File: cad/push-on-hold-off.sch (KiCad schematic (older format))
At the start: 17 parts, among them P1 CONN_01X04, P2 CONN_01X04, Q1 IRF7309IPBF, SW1 SW_PUSH_SMALL

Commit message: Sort button-side of board
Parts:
- LED1, LED2: footprint KiCad/LEDs.pretty:LED_0603 -> KiCad/Resistors_SMD.pretty:R_0603_HandSoldering
- Q1: footprint Housings_SOIC:SOIC-8_3.9x4.9mm_Pitch1.27mm -> KiCad/Housings_SOIC.pretty:SOIC-8_3.9x4.9mm_Pitch1.27mm
- SW1: footprint KiCad/Buttons_Switches_SMD.pretty:SW_SPST_EVPBF -> custom:FSM2JSMA
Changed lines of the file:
@@
 F 0 "Q1" H 5900 4250 50  0000 L CNN
 F 1 "IRF7309IPBF" H 5600 4550 50  0000 L CNN
-F 2 "Housings_SOIC:SOIC-8_3.9x4.9mm_Pitch1.27mm" H 5200 3700 50  0000 L CNN
+F 2 "KiCad/Housings_SOIC.pretty:SOIC-8_3.9x4.9mm_Pitch1.27mm" H 5200 3700 50  0000 L CNN
 F 3 "" H 6050 4400 50  0000 L CNN
 F 4 "2468006" H 6050 4400 60  0001 C CNN "Vendor"
@@
 F 0 "Q1" H 6250 3775 50  0000 L CNN
 F 1 "IRF7309IPBF" H 6250 3700 50  0000 L CNN
-F 2 "Housings_SOIC:SOIC-8_3.9x4.9mm_Pitch1.27mm" H 6250 3625 50  0000 L CNN
+F 2 "KiCad/Housings_SOIC.pretty:SOIC-8_3.9x4.9mm_Pitch1.27mm" H 6250 3625 50  0000 L CNN
 F 3 "" H 6000 3700 50  0000 L CNN
 	2    6000 3700
@@
 $EndComp
 $Comp
-L GND #PWR1
+L GND #PWR01
 U 1 1 569FC7CE
 P 3550 4150
-F 0 "#PWR1" H 3550 3900 50  0001 C CNN
+F 0 "#PWR01" H 3550 3900 50  0001 C CNN
 F 1 "GND" H 3550 4000 50  0000 C CNN
 F 2 "" H 3550 4150 60  0000 C CNN
@@
 $EndComp
 $Comp
-L GND #PWR3
+L GND #PWR02
 U 1 1 569FCD58
 P 5950 4650
-F 0 "#PWR3" H 5950 4400 50  0001 C CNN
+F 0 "#PWR02" H 5950 4400 50  0001 C CNN
 F 1 "GND" H 5950 4500 50  0000 C CNN
 F 2 "" H 5950 4650 60  0000 C CNN
@@
 Button
 $Comp
-L GND #PWR6
+L GND #PWR03
 U 1 1 569FDE5F
 P 7650 4050
-F 0 "#PWR6" H 7650 3800 50  0001 C CNN
+F 0 "#PWR03" H 7650 3800 50  0001 C CNN
 F 1 "GND" H 7650 3900 50  0000 C CNN
 F 2 "" H 7650 4050 60  0000 C CNN
@@
 F 0 "SW1" H 6100 5460 30  0000 C CNN
 F 1 "SW_PUSH_SMALL" H 5950 5271 30  0000 C CNN
-F 2 "KiCad/Buttons_Switches_SMD.pretty:SW_SPST_EVPBF" H 5950 5350 60  0001 C CNN
+F 2 "custom:FSM2JSMA" H 5950 5350 60  0001 C CNN
 F 3 "" H 5950 5350 60  0000 C CNN
 F 4 "3801305" H 5950 5350 60  0001 C CNN "Vendor"
@@
 $EndComp
 $Comp
-L GND #PWR4
+L GND #PWR04
 U 1 1 569FECE2
 P 6100 5500
-F 0 "#PWR4" H 6100 5250 50  0001 C CNN
+F 0 "#PWR04" H 6100 5250 50  0001 C CNN
 F 1 "GND" H 6100 5350 50  0000 C CNN
 F 2 "" H 6100 5500 60  0000 C CNN
@@
 F 0 "LED2" V 7296 4492 50  0000 R CNN
 F 1 "LED" V 7205 4492 50  0000 R CNN
-F 2 "KiCad/LEDs.pretty:LED_0603" H 7250 4600 50  0001 C CNN
+F 2 "KiCad/Resistors_SMD.pretty:R_0603_HandSoldering" H 7250 4600 50  0001 C CNN
 F 3 "" H 7250 4600 50  0000 C CNN
 	1    7250 4600
@@
 F 0 "LED1" V 3796 4742 50  0000 R CNN
 F 1 "LED" V 3705 4742 50  0000 R CNN
-F 2 "KiCad/LEDs.pretty:LED_0603" H 3750 4850 50  0001 C CNN
+F 2 "KiCad/Resistors_SMD.pretty:R_0603_HandSoldering" H 3750 4850 50  0001 C CNN
 F 3 "" H 3750 4850 50  0000 C CNN
 	1    3750 4850
@@
 	3750 4500 3750 4650
 $Comp
-L GND #PWR5
+L GND #PWR05
 U 1 1 57595997
 P 7250 5000
-F 0 "#PWR5" H 7250 4750 50  0001 C CNN
+F 0 "#PWR05" H 7250 4750 50  0001 C CNN
 F 1 "GND" H 7255 4827 50  0000 C CNN
 F 2 "" H 7250 5000 50  0000 C CNN
@@
 $EndComp
 $Comp
-L GND #PWR2
+L GND #PWR06
 U 1 1 575959DF
 P 3750 5150
-F 0 "#PWR2" H 3750 4900 50  0001 C CNN
+F 0 "#PWR06" H 3750 4900 50  0001 C CNN
 F 1 "GND" H 3755 4977 50  0000 C CNN
 F 2 "" H 3750 5150 50  0000 C CNN

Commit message: Switch diode to a mini-melf
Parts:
- D1: footprint KiCad/Diodes_SMD.pretty:SMA_Handsoldering -> KiCad/Diodes_SMD.pretty:MiniMELF_Handsoldering
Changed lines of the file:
@@
 F 0 "D1" H 4000 4600 50  0000 C CNN
 F 1 "D" H 4000 4400 50  0000 C CNN
-F 2 "KiCad/Diodes_SMD.pretty:SMA_Handsoldering" H 4000 4500 60  0001 C CNN
+F 2 "KiCad/Diodes_SMD.pretty:MiniMELF_Handsoldering" H 4000 4500 60  0001 C CNN
 F 3 "" H 4000 4500 60  0000 C CNN
 F 4 "1466524" H 4000 4500 60  0001 C CNN "Vendor"

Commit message: Route the board
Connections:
- net Vin: no longer C4.1, JP1.2
- new net: C4.1, JP1.2
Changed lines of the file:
@@
 	5400 3900 5500 3900
 Connection ~ 5950 3900
-Wire Wire Line
-	5450 3600 5450 3900
 Connection ~ 5450 3900
 Connection ~ 5450 3600

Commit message: Sort out silkscreen and plot
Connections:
- net Vin: now also C4.1, JP1.2
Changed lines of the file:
@@
 	3750 5150 3750 5050
 Connection ~ 3750 3600
+Wire Wire Line
+	5450 3900 5450 3600
 $EndSCHEMATC

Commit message: Update BOM
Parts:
- C1: Description (none) -> 1uF 0603 X5R; Digikey (none) -> 445-1796-1-ND; Farnell (none) -> 2354048; Manufacturer (none) -> TDK; Mouser (none) -> CC0603KRX5R7BB105; Newark (none) -> 04X3188; Part Number (none) -> C0603X5R0J104K030BC; RS (none) -> 7882818
- C2: Description (none) -> 10uF 0603 X5R; Digikey (none) -> 445-6853-1-ND; Farnell (none) -> 2211164; Manufacturer (none) -> TDK; Mouser (none) -> 06036D106MAT2A; Newark (none) -> 04X3239; Part Number (none) -> C1608X5R1A106M080AC; RS (none) -> 7882893
- D1: Farnell (none) -> 7355513; Manufacturer (none) -> MULTICOMP; Part Number (none) -> LL4148
- Q1: Digikey (none) -> IRF7309PBFCT-ND; Farnell (none) -> 2468006; Manufacturer (none) -> International Rectifier; Mouser (none) -> IRF7309PBF; Newark (none) -> 19K8239; Part Number (none) -> IRF7309PBF; RS (none) -> 5429377
- R1: Description (none) -> 10k 0603; Digikey (none) -> 541-10KGCT-ND; Farnell (none) -> 1469749; Manufacturer (none) -> Vishay; Mouser (none) -> CRCW060310K0JNEAHP; Newark (none) -> 52K8066; Part Number (none) -> CRCW060310K0JNEA; RS (none) -> 8206928
- R2: Description (none) -> 100k 0603; Digikey (none) -> 541-100KGCT-ND; Farnell (none) -> 1692517; Manufacturer (none) -> Vishay; Mouser (none) -> CRCW0603100KJNEAHP; Newark (none) -> 59M6763; Part Number (none) -> CRCW0603100KJNEA; RS (none) -> 8206916
- R3: Description (none) -> 300k 0603; Digikey (none) -> 311-300KGRCT-ND; Farnell (none) -> 1652871; Manufacturer (none) -> Vishay; Mouser (none) -> RC0603JR07300KL; Newark (none) -> 52K8409; Part Number (none) -> CRCW0603300KFKEA; RS (none) -> 8280617
- SW1: Digikey (none) -> 450-1129-ND; Farnell (none) -> 3801305; Manufacturer (none) -> TE Connectivity; Mouser (none) -> 414375651; Newark (none) -> 93K3887; Part Number (none) -> 4-1437565-1; RS (none) -> 4791508

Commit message: Extract bom into schematic
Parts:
- C1: Digikey 445-1796-1-ND -> 490-3290-1-ND; Farnell 2354048 -> 1828900; MPN (none) -> GRM188R71E224KA88D; Manufacturer TDK -> Murata; Mouser CC0603KRX5R7BB105 -> GRM188R71E224KA88D; Newark 04X3188 -> 91R0949; Qty (none) -> 1; RS 7882818 -> 6242496
- C2: MPN (none) -> C1608X5R1A106M080AC; Qty (none) -> 1
- C4: Description (none) -> 0.1uF 0603 X5R; Digikey (none) -> 399-5089-1-ND; Farnell (none) -> 1288255; MPN (none) -> C0603C104K5RACTU; Manufacturer (none) -> Kemet; Mouser (none) -> C0603C104K5RACTU; Newark (none) -> 72J5992; Qty (none) -> 1; RS (none) -> 8015347
- D1: Description (none) -> Diode MiniMELF; Digikey (none) -> LL4148FSCT-ND; MPN (none) -> LL4148; Manufacturer MULTICOMP -> (none); Mouser (none) -> LL4148; Newark (none) -> 14M6003; Qty (none) -> 1; RS (none) -> 6708826
- LED1, LED2: Description (none) -> 0603 20mA yellow; Digikey (none) -> 511-1582-1-ND; Farnell (none) -> 1465989; MPN (none) -> SML-D12Y8WT86; Manufacturer (none) -> Rohm; Mouser (none) -> 5988150107F; Newark (none) -> 75R0585; Qty (none) -> 2; RS (none) -> 7008023
- Q1: Description (none) -> 30V Vds, 3A Id, Dual HEXFET MOSFET; MPN (none) -> IRF7309PBF; Qty (none) -> 1
- R1: MPN (none) -> CRCW060310K0JNEA; Qty (none) -> 1
- R2: MPN (none) -> CRCW0603100KJNEA; Qty (none) -> 2
- R3: MPN (none) -> CRCW0603300KFKEA; Qty (none) -> 1
- R4: Description (none) -> 100k 0603; Digikey (none) -> 541-100KGCT-ND; Farnell (none) -> 1692517; MPN (none) -> CRCW0603100KJNEA; Manufacturer (none) -> Vishay; Mouser (none) -> CRCW0603100KJNEAHP; Newark (none) -> 59M6763; Qty (none) -> 2; RS (none) -> 8206916
- R5: Description (none) -> 1k 0603; Digikey (none) -> 311-1.00KCRCT-ND; Farnell (none) -> 9237496; MPN (none) -> RC0805FR-071KL; Manufacturer (none) -> Yageo; Mouser (none) -> RC0805FR071KL; Newark (none) -> 82K7536; Qty (none) -> 2; RS (none) -> 6183583
- SW1: Description (none) -> Tactile switch; Digikey 450-1129-ND -> 450-1130-ND; Farnell 3801305 -> 3801287; MPN (none) -> FSM2JSMA; Manufacturer TE Connectivity -> (none); Mouser 414375651 -> 214375657; Newark 93K3887 -> 92F2864; Qty (none) -> 1; RS 4791508 -> 4791491

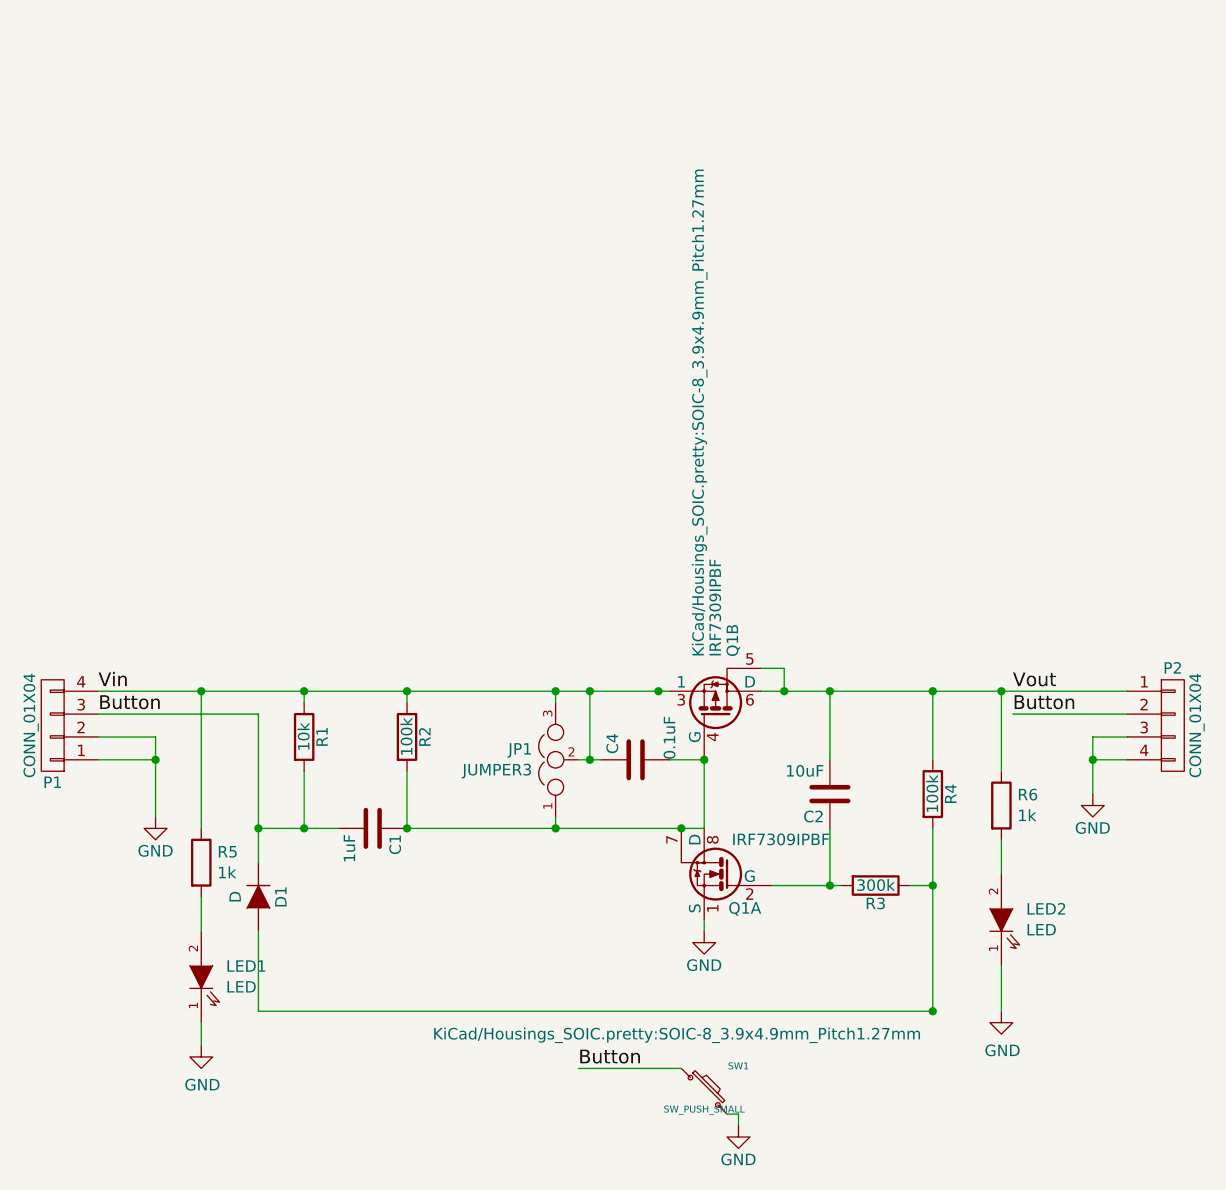
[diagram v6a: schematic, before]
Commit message: Fix auto-on jumper which was supposed to be to ground
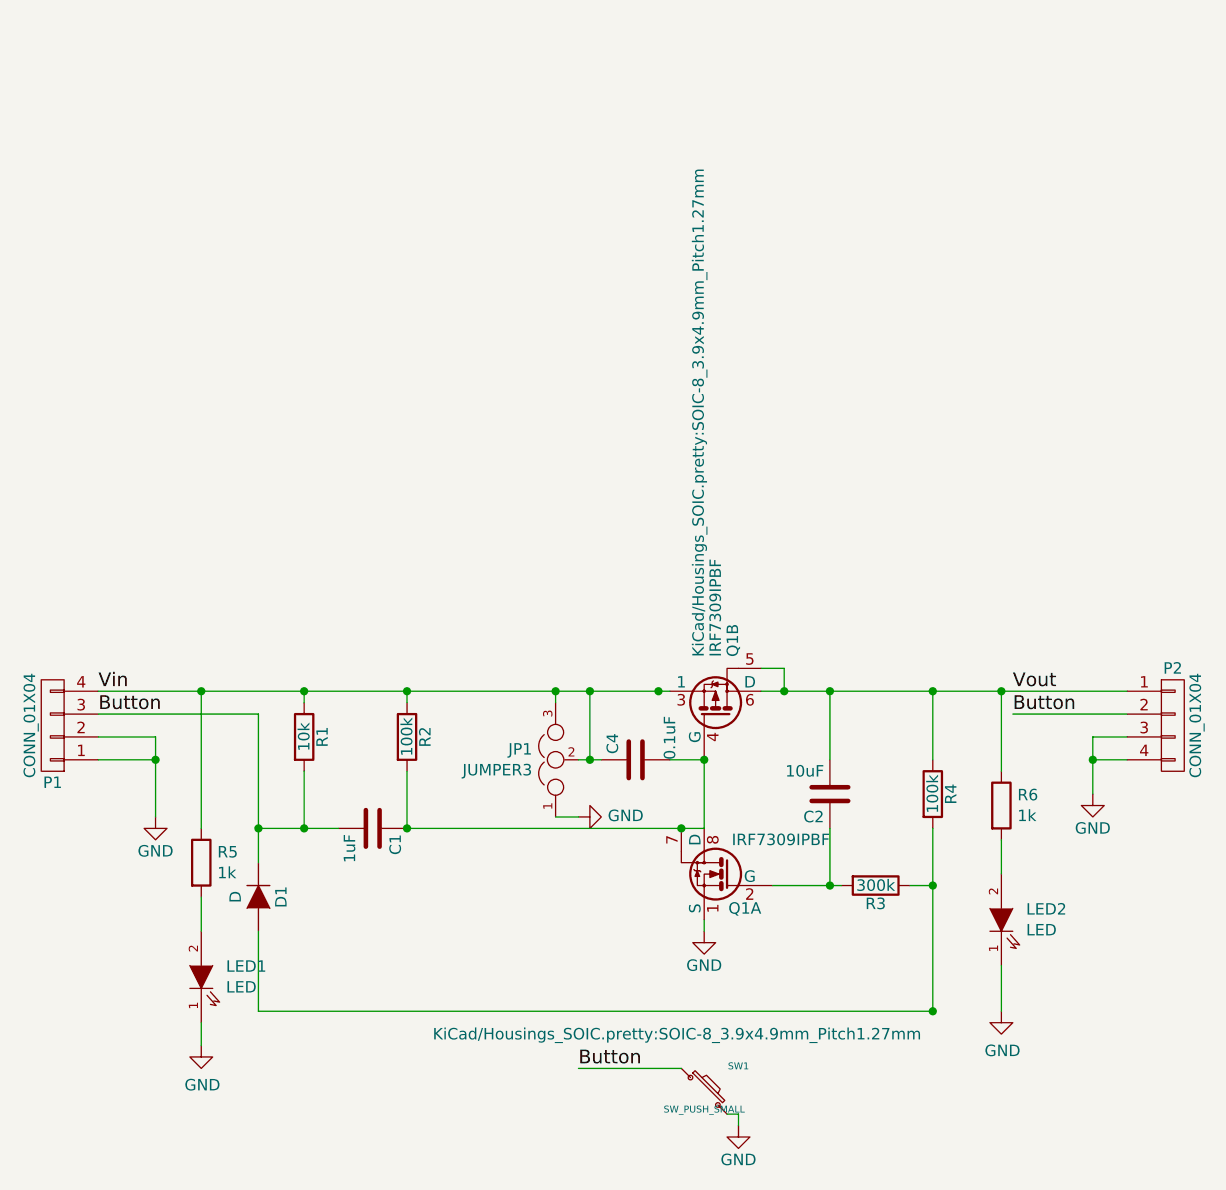
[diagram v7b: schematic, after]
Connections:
- net GND: now also JP1.1
- net at C1.1, C4.2, Q1.4 (G)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: no longer JP1.1
